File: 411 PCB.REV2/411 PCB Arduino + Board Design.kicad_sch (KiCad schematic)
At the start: 28 parts, among them J1 ICSP CONN, J2 Conn_01x06_MountingPin, J4 Conn_01x04, Q1 Q_NMOS_GDS, SW1 SW_SPST, SW3 SW_MEC_5E, U1 ATmega328P-P, Y1 8 MHz

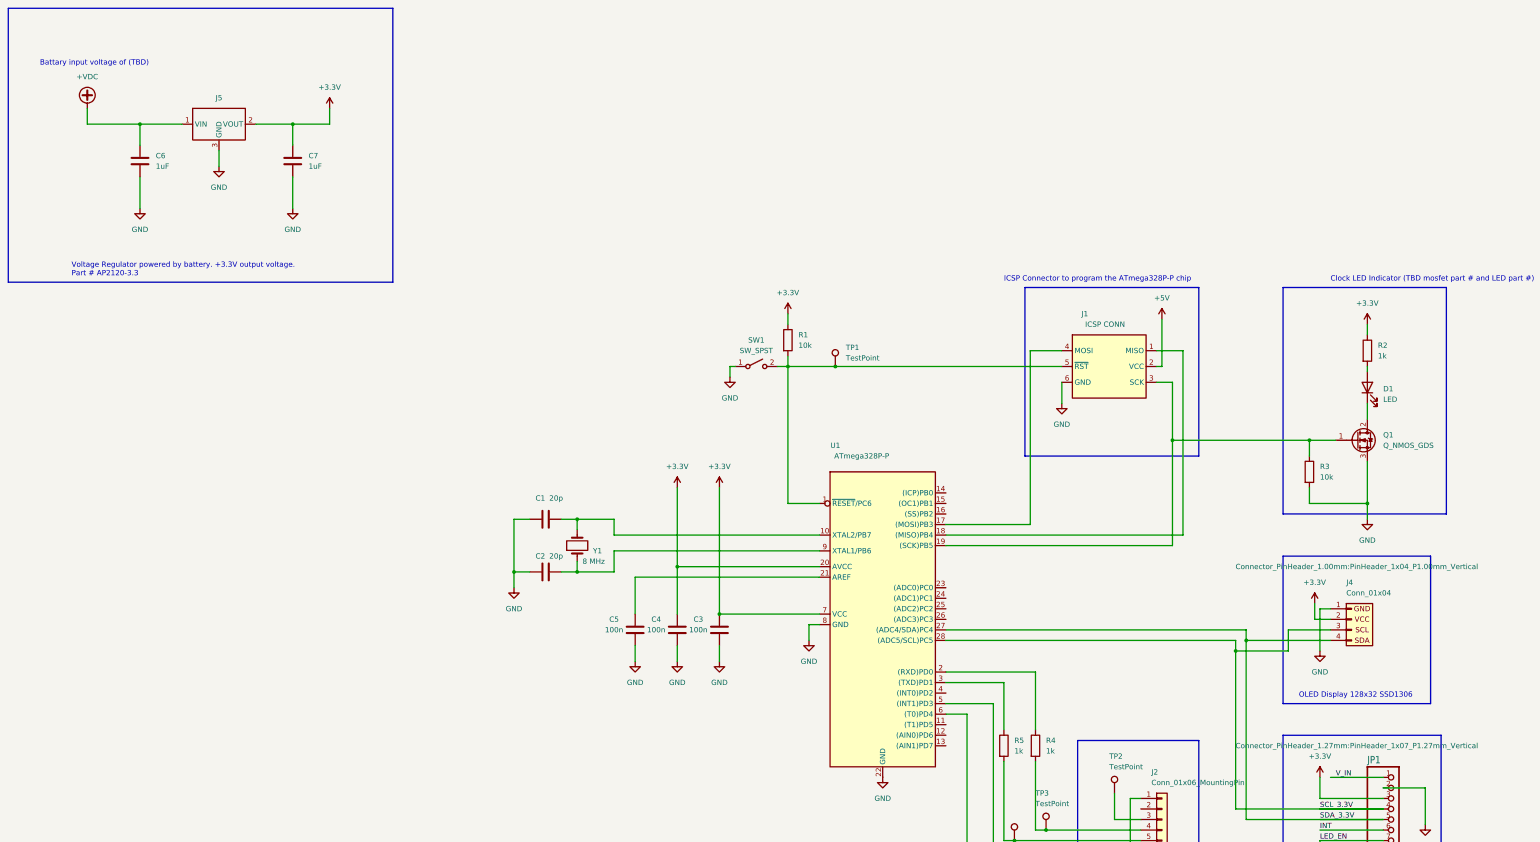
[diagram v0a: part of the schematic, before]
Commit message: Updated values and descriptions on Schematic
Changed the capacitor values for the 8MHz clock from 20pF to 10pF. Added the Max current consumption of the color sensor, display, LED, and ATmega328P-PN. Also added the Max Current output for the Voltage Regulator. Changes power source to Voltage regulator to Battery Management System.
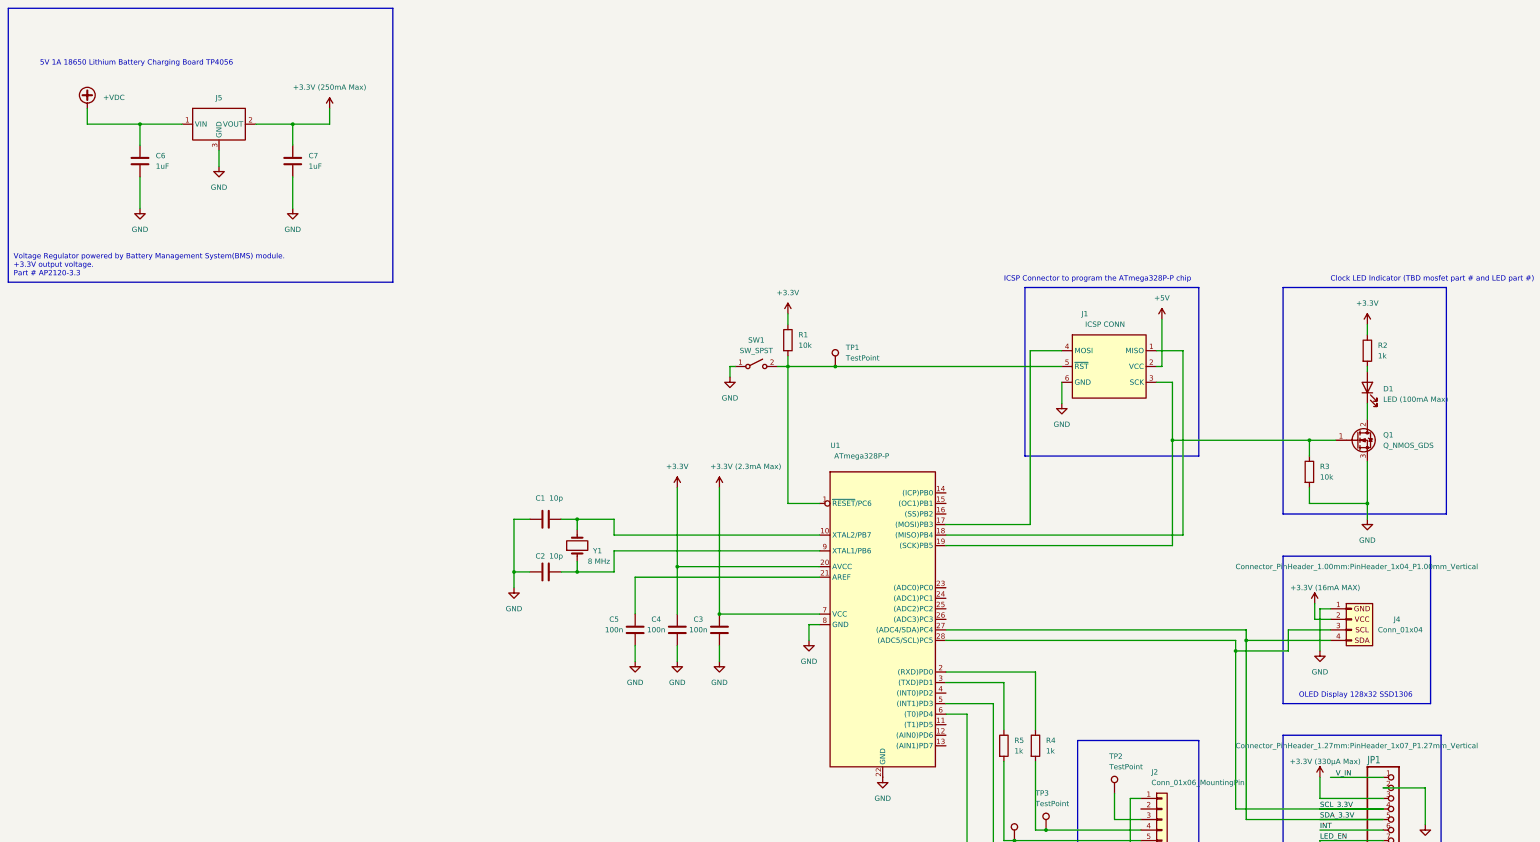
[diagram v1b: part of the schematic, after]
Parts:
- C1, C2: value 20p -> 10p
- D1: value LED -> LED (100mA Max)
- Y1: value 8 MHz -> 8 MHz
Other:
- note added: "5V 1A 18650 Lithium Battery Charging Board TP4056"
- note added: "Voltage Regulator powered by Battery Management System(BMS) module. +3.3V output voltage. Part # AP2120-3.3"
- note removed: "Battary input voltage of (TBD)"
- note removed: "Voltage Regulator powered by battery. +3.3V output voltage. Part # AP2120-3.3"
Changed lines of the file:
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@@
     (effects (font (size 1.27 1.27)) (justify left bottom))
   )
-  (text "Battary input voltage of (TBD)" (at 97.79 118.11 0)
+  (text "5V 1A 18650 Lithium Battery Charging Board TP4056" (at 97.79 118.11 0)
     (effects (font (size 1.27 1.27)) (justify left bottom))
   )
@@
     (effects (font (size 1.27 1.27)) (justify left bottom))
   )
-  (text "Voltage Regulator powered by battery. +3.3V output voltage.\nPart # AP2120-3.3"
-    (at 105.41 168.91 0)
+  (text "Voltage Regulator powered by Battery Management System(BMS) module.\n+3.3V output voltage.\nPart # AP2120-3.3"
+    (at 91.44 168.91 0)
     (effects (font (size 1.27 1.27)) (justify left bottom))
   )
@@
       (effects (font (size 1.27 1.27)) (justify right))
     )
-    (property "Value" "8 MHz" (at 228.6 237.49 90)
+    (property "Value" "8 MHz " (at 229.87 237.49 90)
       (effects (font (size 1.27 1.27)) (justify right))
     )
@@
       (effects (font (size 1.27 1.27)) (justify right))
     )
-    (property "Value" "LED" (at 421.64 198.4375 90)
+    (property "Value" "LED (100mA Max)" (at 421.64 198.4375 90)
       (effects (font (size 1.27 1.27)) (justify right))
     )
@@
     )
   )
-  (symbol (lib_id "power:+3.3V") (at 405.13 247.65 0) (unit 1)
-    (in_bom yes) (on_board yes) (dnp no) (fields_autoplaced)
+  (symbol (lib_name "+3.3V_3") (lib_id "power:+3.3V") (at 405.13 247.65 0) (unit 1)
+    (in_bom yes) (on_board yes) (dnp no)
     (property "Reference" "#PWR019" (at 405.13 251.46 0)
       (effects (font (size 1.27 1.27)) hide)
     )
-    (property "Value" "+3.3V" (at 405.13 242.57 0)
+    (property "Value" "+3.3V (16mA MAX)" (at 407.67 243.84 0)
       (effects (font (size 1.27 1.27)))
     )
@@
       (effects (font (size 1.27 1.27)))
     )
-    (property "Value" "20p" (at 222.25 222.25 90)
+    (property "Value" "10p" (at 222.25 222.25 90)
       (effects (font (size 1.27 1.27)))
     )
@@
     )
   )
-  (symbol (lib_id "power:+3.3V") (at 406.4 289.56 0) (unit 1)
-    (in_bom yes) (on_board yes) (dnp no) (fields_autoplaced)
+  (symbol (lib_name "+3.3V_2") (lib_id "power:+3.3V") (at 406.4 289.56 0) (unit 1)
+    (in_bom yes) (on_board yes) (dnp no)
     (property "Reference" "#PWR016" (at 406.4 293.37 0)
       (effects (font (size 1.27 1.27)) hide)
     )
-    (property "Value" "+3.3V" (at 406.4 284.48 0)
+    (property "Value" "+3.3V (330µA Max)" (at 407.67 285.75 0)
       (effects (font (size 1.27 1.27)))
     )
@@
     )
   )
-  (symbol (lib_id "power:+3.3V") (at 167.64 128.27 0) (unit 1)
+  (symbol (lib_name "+3.3V_1") (lib_id "power:+3.3V") (at 167.64 128.27 0) (unit 1)
     (in_bom yes) (on_board yes) (dnp no) (fields_autoplaced)
     (property "Reference" "#PWR024" (at 167.64 132.08 0)
       (effects (font (size 1.27 1.27)) hide)
     )
-    (property "Value" "+3.3V" (at 167.64 123.19 0)
+    (property "Value" "+3.3V (250mA Max)" (at 167.64 123.19 0)
       (effects (font (size 1.27 1.27)))
     )
@@
     )
   )
-  (symbol (lib_id "power:+3.3V") (at 261.62 219.71 0) (unit 1)
-    (in_bom yes) (on_board yes) (dnp no) (fields_autoplaced)
+  (symbol (lib_name "+3.3V_4") (lib_id "power:+3.3V") (at 261.62 219.71 0) (unit 1)
+    (in_bom yes) (on_board yes) (dnp no)
     (property "Reference" "#PWR05" (at 261.62 223.52 0)
       (effects (font (size 1.27 1.27)) hide)
     )
-    (property "Value" "+3.3V" (at 261.62 214.63 0)
+    (property "Value" "+3.3V (2.3mA Max)" (at 267.97 214.63 0)
       (effects (font (size 1.27 1.27)))
     )
@@
   (symbol (lib_id "Connector_Generic:Conn_01x04") (at 414.02 251.46 0) (unit 1)
     (in_bom yes) (on_board yes) (dnp no)
-    (property "Reference" "J4" (at 412.75 242.57 0)
-      (effects (font (size 1.27 1.27)) (justify left))
-    )
-    (property "Value" "Conn_01x04" (at 412.75 245.11 0)
+    (property "Reference" "J4" (at 424.18 251.46 0)
+      (effects (font (size 1.27 1.27)) (justify left))
+    )
+    (property "Value" "Conn_01x04" (at 420.37 254 0)
       (effects (font (size 1.27 1.27)) (justify left))
     )
@@
       (effects (font (size 1.27 1.27)) hide)
     )
-    (property "Value" "+VDC" (at 109.22 120.65 0)
-      (effects (font (size 1.27 1.27)))
+    (property "Value" "+VDC" (at 113.03 125.6665 0)
+      (effects (font (size 1.27 1.27)) (justify left))
     )
     (property "Footprint" "" (at 109.22 128.27 0)
@@
       (effects (font (size 1.27 1.27)))
     )
-    (property "Value" "20p" (at 222.25 236.22 90)
-      (effects (font (size 1.27 1.27)))
-    )
+    (property "Value" "10p" (at 222.25 236.22 90)
+      (effects (font (size 1.27 1.27)))
+    )

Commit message: update
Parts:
- added TP5, TP6: TestPoint, Connector_PinHeader_1.00mm:PinHeader_1x01_P1.00mm_Vertical, symbol Connector:TestPoint
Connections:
- net SCL_3.3V: now also TP5.1
- net SDA_3.3V: now also TP6.1
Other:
- note added: "Clock LED Indicator"
- note added: "USB to Serial Connector"
- note removed: "Clock LED Indicator (TBD mosfet part # and LED part #)"
- note removed: "USB to Serial Connector (to be determined part #)"
- moved on the sheet: C6, C7, J5
